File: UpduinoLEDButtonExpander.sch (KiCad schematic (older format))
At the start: 23 parts, among them J1 Upduino2, J2 Upduino2, J3 Upduino2, SW1 BTN, SW2 BTN, SW3 BTN, SW4 BTN

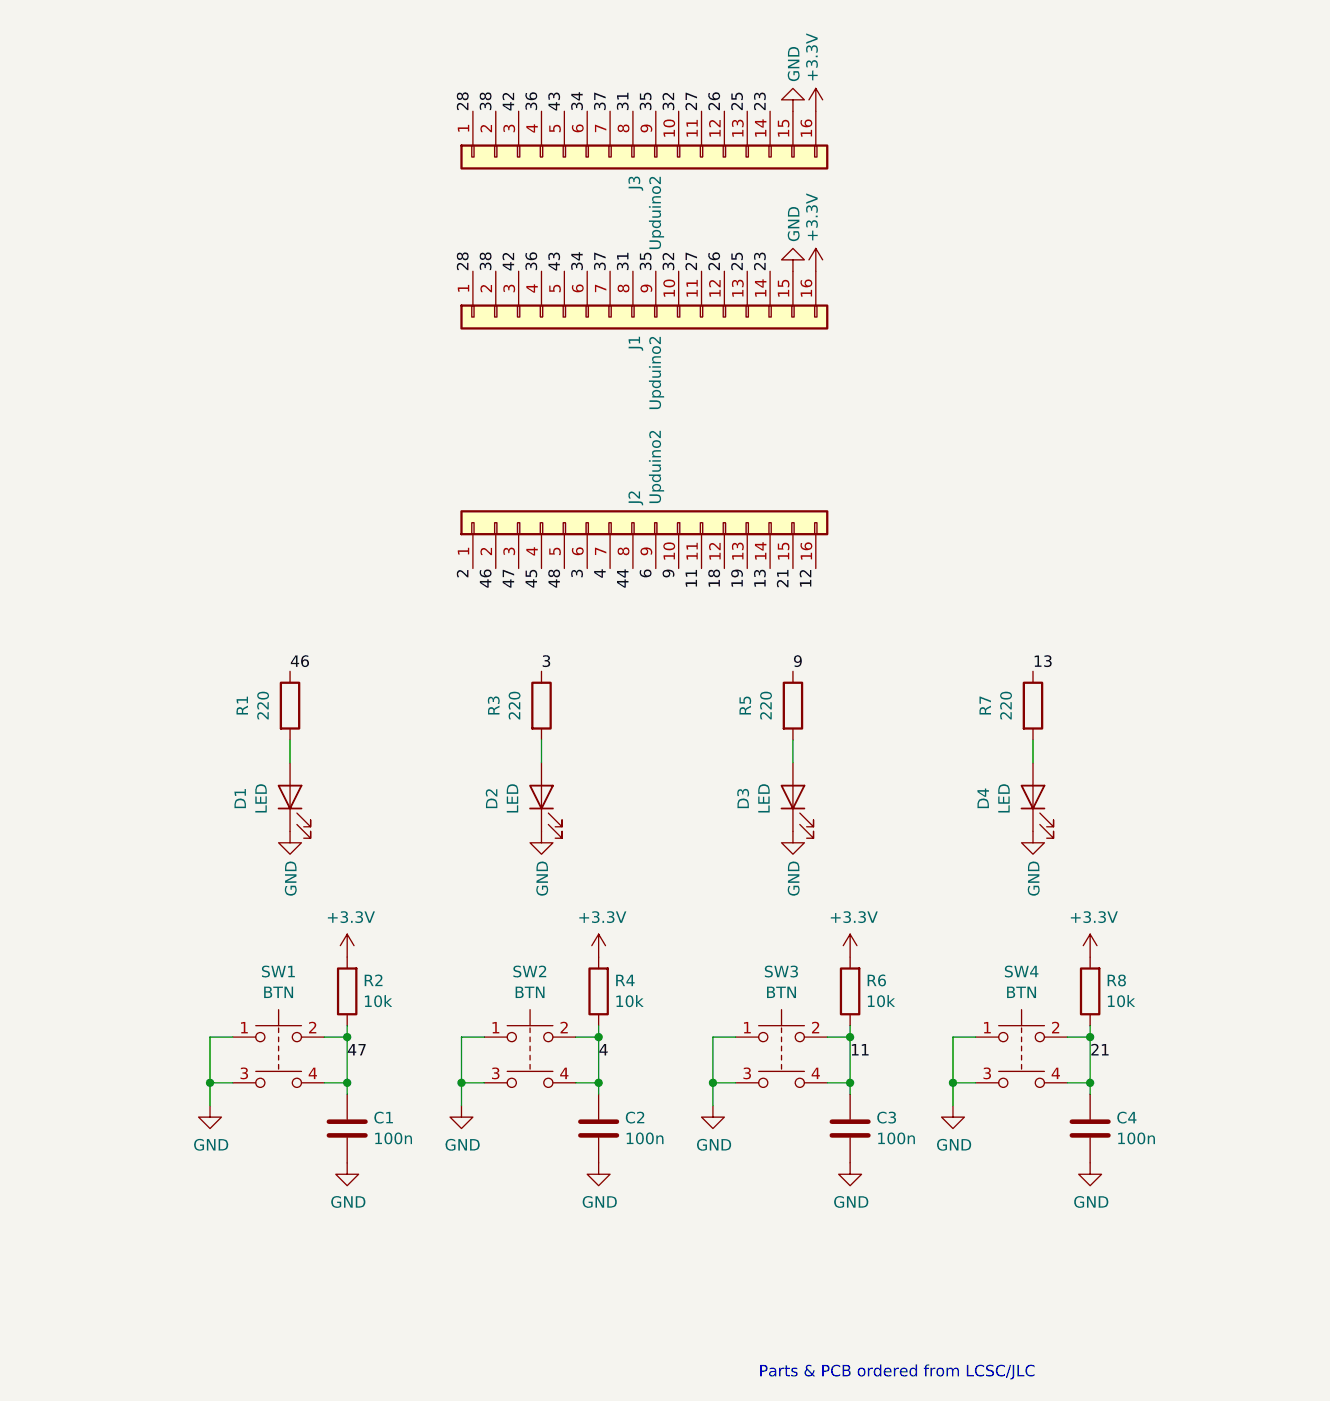
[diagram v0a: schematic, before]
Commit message: Added additional protection resistor for the buttons
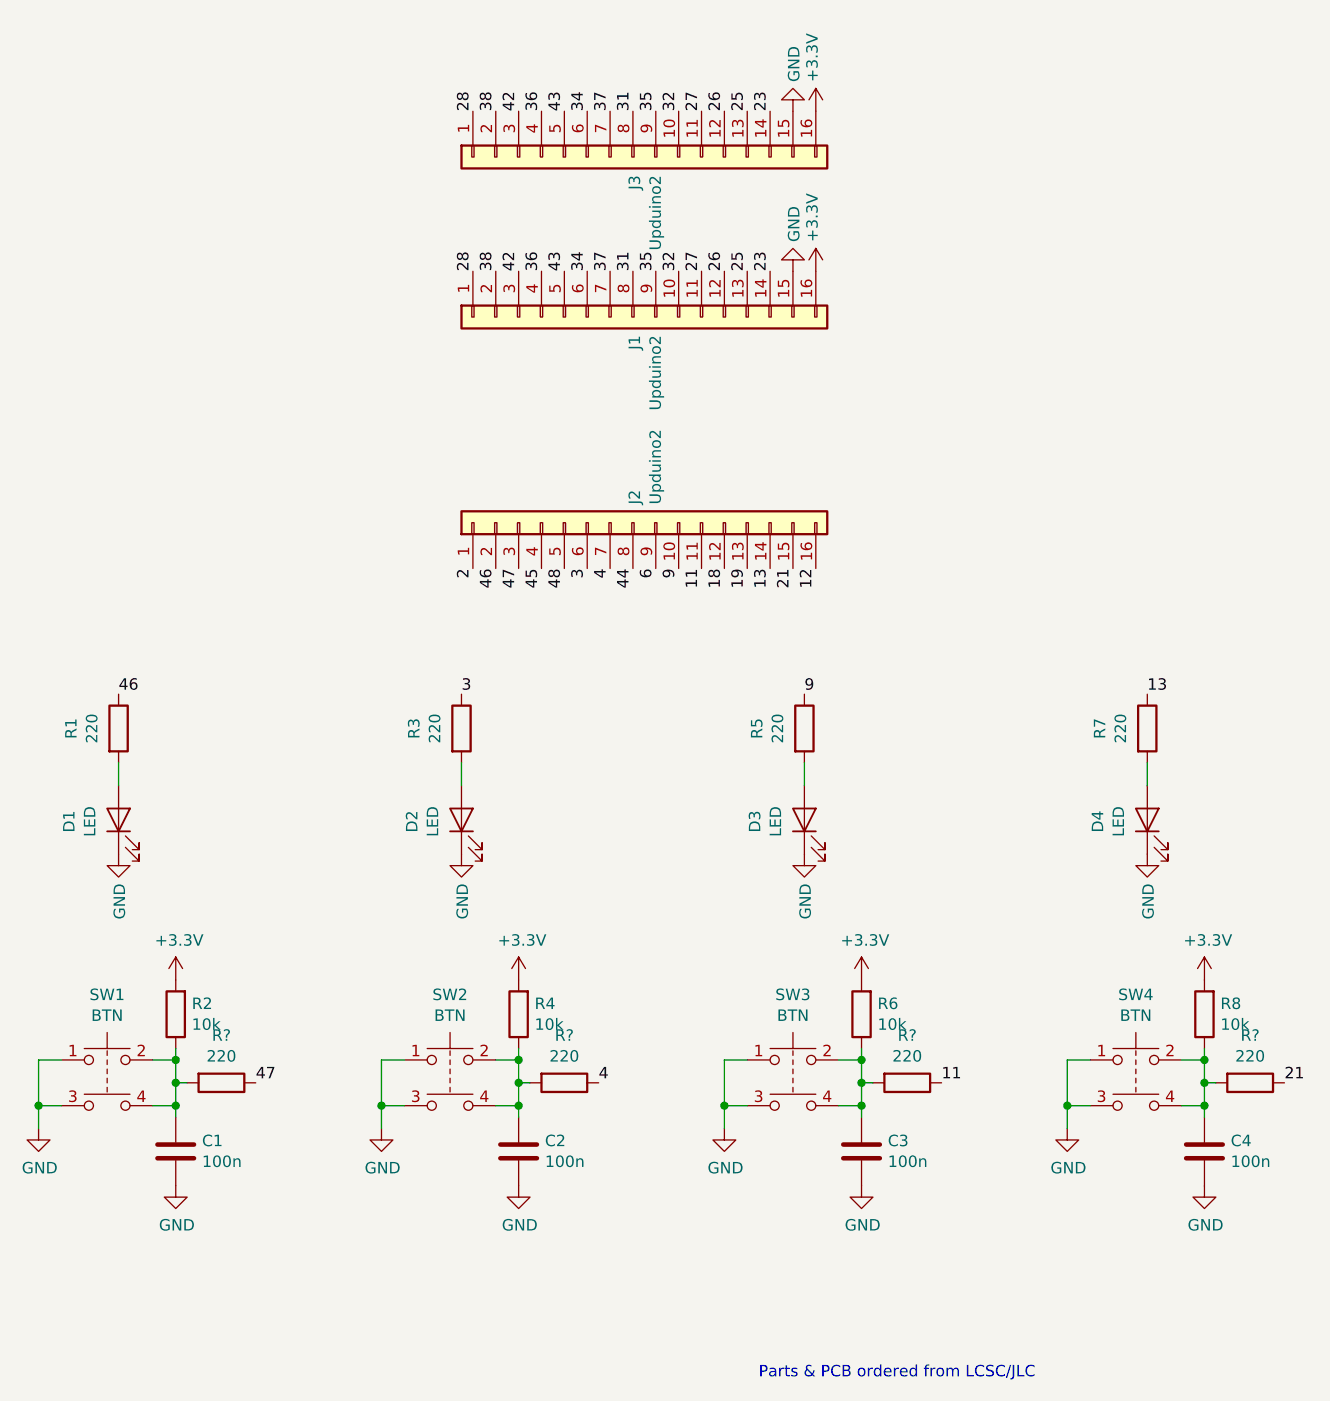
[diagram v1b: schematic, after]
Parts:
- added R? (x4): 220, Resistor_SMD:R_0603_1608Metric_Pad1.05x0.95mm_HandSolder, symbol Device:R
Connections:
- net 11: now also R?.1; no longer C3.1, R6.1, SW3.2, SW3.4
- net 21: now also R?.1; no longer C4.1, R8.1, SW4.2, SW4.4
- net 4: now also R?.1; no longer C2.1, R4.1, SW2.2, SW2.4
- net 47: now also R?.1; no longer C1.1, R2.1, SW1.2, SW1.4
- new net: C1.1, R2.1, R?.2, SW1.2, SW1.4
- new net: C2.1, R4.1, R?.2, SW2.2, SW2.4
- new net: C3.1, R6.1, R?.2, SW3.2, SW3.4
- new net: C4.1, R8.1, R?.2, SW4.2, SW4.4
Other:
- moved on the sheet: C1, C2, C3, C4, D1, D2, D3, D4, R1, R2, R3, R4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

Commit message: Updated pdf files
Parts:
- gave numbers to parts that had none: 4
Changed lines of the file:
@@
 Parts & PCB ordered from LCSC/JLC
 $Comp
-L Device:R R?
+L Device:R R9
 U 1 1 5D933051
 P 4700 5400
-F 0 "R?" V 4493 5400 50  0000 C CNN
+F 0 "R9" V 4493 5400 50  0000 C CNN
 F 1 "220" V 4584 5400 50  0000 C CNN
 F 2 "Resistor_SMD:R_0603_1608Metric_Pad1.05x0.95mm_HandSolder" V 4630 5400 50  0001 C CNN
@@
 $EndComp
 $Comp
-L Device:R R?
+L Device:R R10
 U 1 1 5D935C6D
 P 6200 5400
-F 0 "R?" V 5993 5400 50  0000 C CNN
+F 0 "R10" V 5993 5400 50  0000 C CNN
 F 1 "220" V 6084 5400 50  0000 C CNN
 F 2 "Resistor_SMD:R_0603_1608Metric_Pad1.05x0.95mm_HandSolder" V 6130 5400 50  0001 C CNN
@@
 $EndComp
 $Comp
-L Device:R R?
+L Device:R R11
 U 1 1 5D936136
 P 7700 5400
-F 0 "R?" V 7493 5400 50  0000 C CNN
+F 0 "R11" V 7493 5400 50  0000 C CNN
 F 1 "220" V 7584 5400 50  0000 C CNN
 F 2 "Resistor_SMD:R_0603_1608Metric_Pad1.05x0.95mm_HandSolder" V 7630 5400 50  0001 C CNN
@@
 $EndComp
 $Comp
-L Device:R R?
+L Device:R R12
 U 1 1 5D9364DF
 P 9200 5400
-F 0 "R?" V 8993 5400 50  0000 C CNN
+F 0 "R12" V 8993 5400 50  0000 C CNN
 F 1 "220" V 9084 5400 50  0000 C CNN
 F 2 "Resistor_SMD:R_0603_1608Metric_Pad1.05x0.95mm_HandSolder" V 9130 5400 50  0001 C CNN

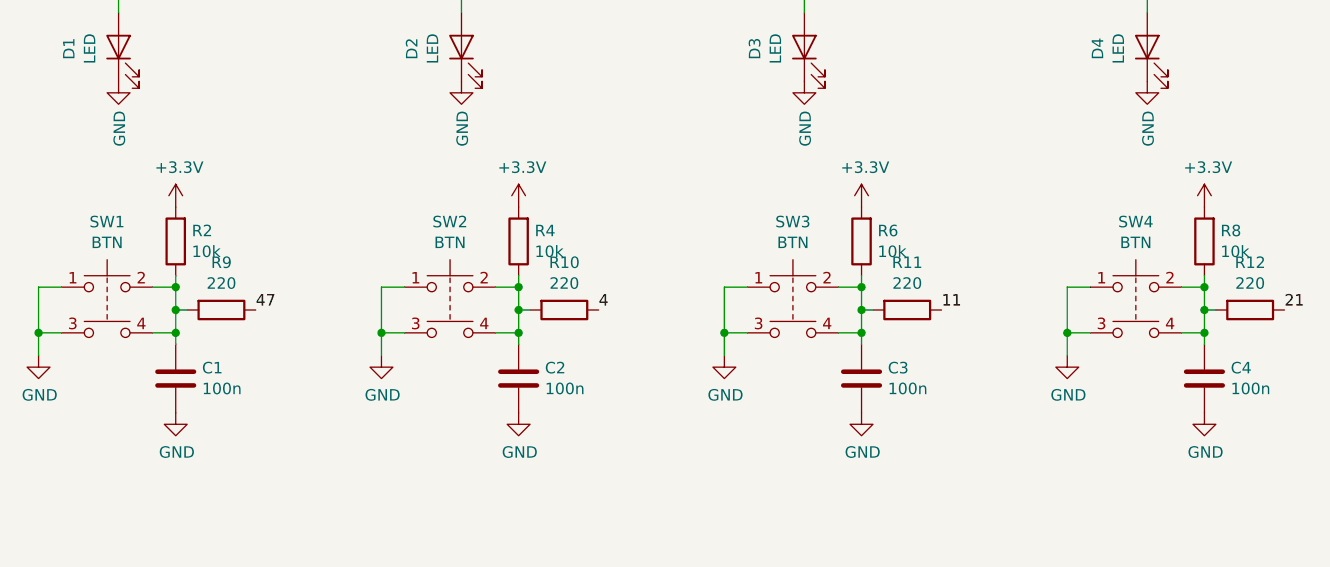
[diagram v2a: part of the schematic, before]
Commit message: Corrected button symbol, added more labels
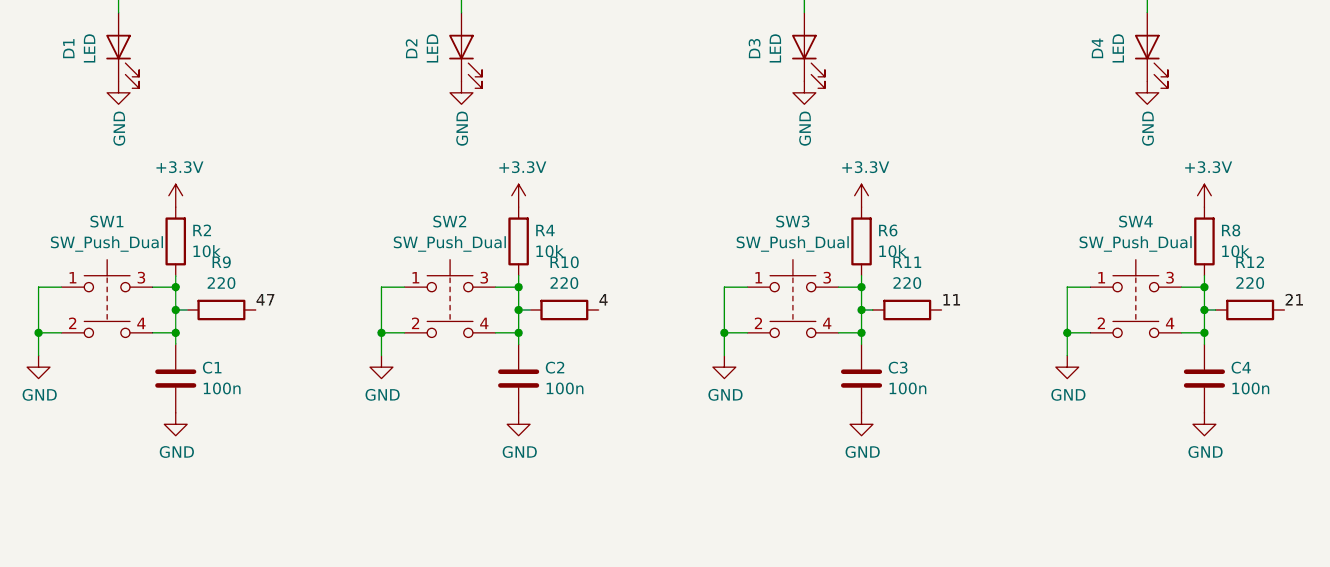
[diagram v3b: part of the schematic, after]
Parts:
- removed SW1, SW2, SW3, SW4: BTN, Button_Switch_THT:SW_TH_Tactile_Omron_B3F-10xx, symbol Switch:SW_Push_Dual
- added SW1, SW2, SW3, SW4: SW_Push_Dual, Button_Switch_THT:SW_TH_Tactile_Omron_B3F-10xx, symbol UpduinoLEDButtonExpander:SW_Push_Dual
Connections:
- net GND: now also SW1.1, SW1.2, SW2.1, SW2.2, SW3.1, SW3.2, SW4.1, SW4.2
- net at C1.1, R2.1, R9.2: now also SW1.3, SW1.4
- net at C2.1, R10.2, R4.1: now also SW2.3, SW2.4
- net at C3.1, R11.2, R6.1: now also SW3.3, SW3.4
- net at C4.1, R12.2, R8.1: now also SW4.3, SW4.4
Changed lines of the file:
@@
-$EndComp
-$Comp
-L Switch:SW_Push_Dual SW1
-U 1 1 5D8C10AD
-P 4200 5300
-F 0 "SW1" H 4200 5585 50  0000 C CNN
-F 1 "BTN" H 4200 5494 50  0000 C CNN
-F 2 "Button_Switch_THT:SW_TH_Tactile_Omron_B3F-10xx" H 4200 5500 50  0001 C CNN
-F 3 "~" H 4200 5500 50  0001 C CNN
-F 4 "K2-1102DP-C4SW-04" H 4200 5300 50  0001 C CNN "MPN"
-	1    4200 5300
-	1    0    0    -1
 $EndComp
 $Comp
@@
 $EndComp
 $Comp
-L Switch:SW_Push_Dual SW2
-U 1 1 5D941202
-P 5700 5300
-F 0 "SW2" H 5700 5585 50  0000 C CNN
-F 1 "BTN" H 5700 5494 50  0000 C CNN
-F 2 "Button_Switch_THT:SW_TH_Tactile_Omron_B3F-10xx" H 5700 5500 50  0001 C CNN
-F 3 "~" H 5700 5500 50  0001 C CNN
-F 4 "K2-1102DP-C4SW-04" H 5700 5300 50  0001 C CNN "MPN"
-	1    5700 5300
-	1    0    0    -1
-$EndComp
-$Comp
 L power:GND #PWR05
 U 1 1 5D941208
@@
 $EndComp
 $Comp
-L Switch:SW_Push_Dual SW3
-U 1 1 5D94394A
-P 7200 5300
-F 0 "SW3" H 7200 5585 50  0000 C CNN
-F 1 "BTN" H 7200 5494 50  0000 C CNN
-F 2 "Button_Switch_THT:SW_TH_Tactile_Omron_B3F-10xx" H 7200 5500 50  0001 C CNN
-F 3 "~" H 7200 5500 50  0001 C CNN
-F 4 "K2-1102DP-C4SW-04" H 7200 5300 50  0001 C CNN "MPN"
-	1    7200 5300
-	1    0    0    -1
-$EndComp
-$Comp
 L power:GND #PWR09
 U 1 1 5D943950
@@
 F 4 " RS-03K221JT" H 8750 3850 50  0001 C CNN "MPN"
 	1    8750 3850
-	1    0    0    -1
-$EndComp
-$Comp
-L Switch:SW_Push_Dual SW4
-U 1 1 5D944F92
-P 8700 5300
-F 0 "SW4" H 8700 5585 50  0000 C CNN
-F 1 "BTN" H 8700 5494 50  0000 C CNN
-F 2 "Button_Switch_THT:SW_TH_Tactile_Omron_B3F-10xx" H 8700 5500 50  0001 C CNN
-F 3 "~" H 8700 5500 50  0001 C CNN
-F 4 "K2-1102DP-C4SW-04" H 8700 5300 50  0001 C CNN "MPN"
-	1    8700 5300
 	1    0    0    -1
 $EndComp
@@
 Wire Wire Line
 	9000 5400 9000 5300
+$Comp
+L UpduinoLEDButtonExpander:SW_Push_Dual SW1
+U 1 1 5DA46FF8
+P 4200 5300
+F 0 "SW1" H 4200 5585 50  0000 C CNN
+F 1 "SW_Push_Dual" H 4200 5494 50  0000 C CNN
+F 2 "Button_Switch_THT:SW_TH_Tactile_Omron_B3F-10xx" H 4200 5500 50  0001 C CNN
+F 3 "~" H 4200 5500 50  0001 C CNN
+	1    4200 5300
+	1    0    0    -1
+$EndComp
+$Comp
+L UpduinoLEDButtonExpander:SW_Push_Dual SW2
+U 1 1 5DA47B4F
+P 5700 5300
+F 0 "SW2" H 5700 5585 50  0000 C CNN
+F 1 "SW_Push_Dual" H 5700 5494 50  0000 C CNN
+F 2 "Button_Switch_THT:SW_TH_Tactile_Omron_B3F-10xx" H 5700 5500 50  0001 C CNN
+F 3 "~" H 5700 5500 50  0001 C CNN
+	1    5700 5300
+	1    0    0    -1
+$EndComp
+$Comp
+L UpduinoLEDButtonExpander:SW_Push_Dual SW3
+U 1 1 5DA483E6
+P 7200 5300
+F 0 "SW3" H 7200 5585 50  0000 C CNN
+F 1 "SW_Push_Dual" H 7200 5494 50  0000 C CNN
+F 2 "Button_Switch_THT:SW_TH_Tactile_Omron_B3F-10xx" H 7200 5500 50  0001 C CNN
+F 3 "~" H 7200 5500 50  0001 C CNN
+	1    7200 5300
+	1    0    0    -1
+$EndComp
+$Comp
+L UpduinoLEDButtonExpander:SW_Push_Dual SW4
+U 1 1 5DA48C7E
+P 8700 5300
+F 0 "SW4" H 8700 5585 50  0000 C CNN
+F 1 "SW_Push_Dual" H 8700 5494 50  0000 C CNN
+F 2 "Button_Switch_THT:SW_TH_Tactile_Omron_B3F-10xx" H 8700 5500 50  0001 C CNN
+F 3 "~" H 8700 5500 50  0001 C CNN
+	1    8700 5300
+	1    0    0    -1
+$EndComp
 $EndSCHEMATC
